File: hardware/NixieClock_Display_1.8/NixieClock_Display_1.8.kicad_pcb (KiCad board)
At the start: 2 copper layers, 31.6 x 46 mm, 2 parts, among them J1 Conn_01x14, J2 Conn_01x14

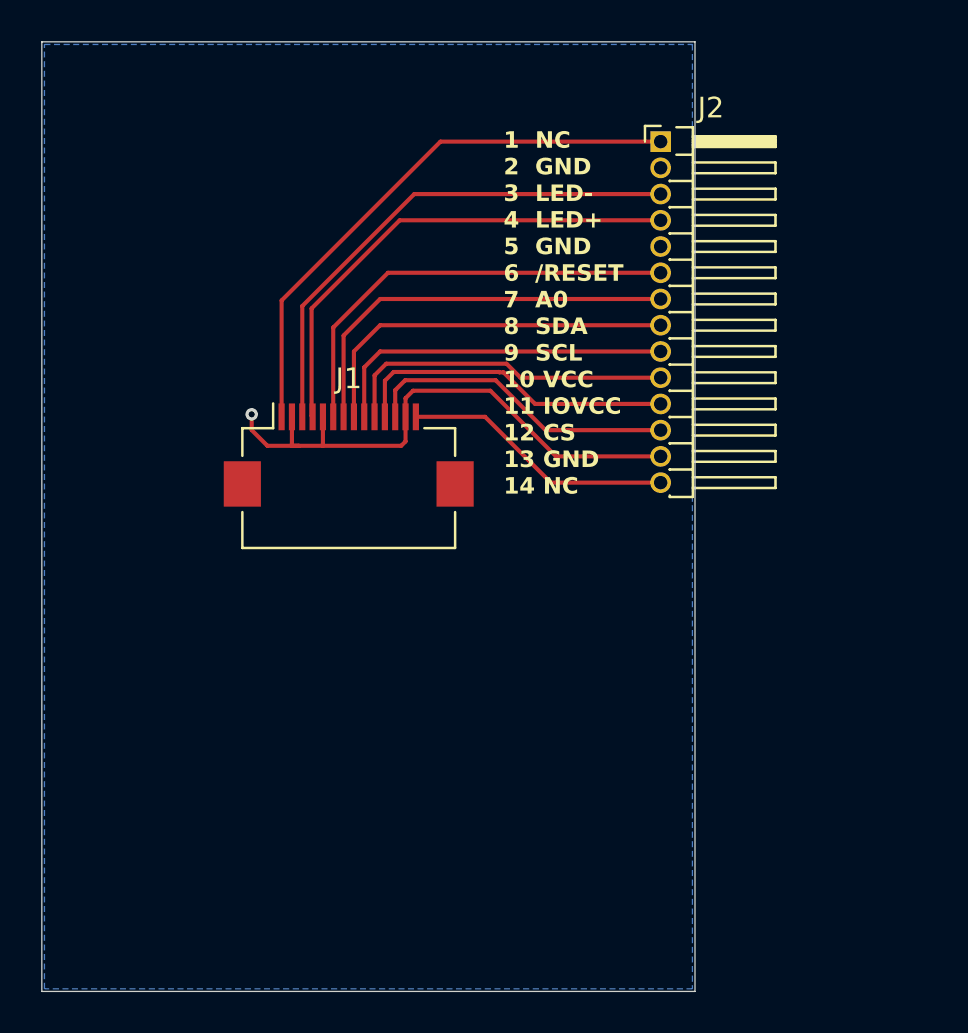
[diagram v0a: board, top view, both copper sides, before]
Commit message: schaltplan für mainboard angelegt
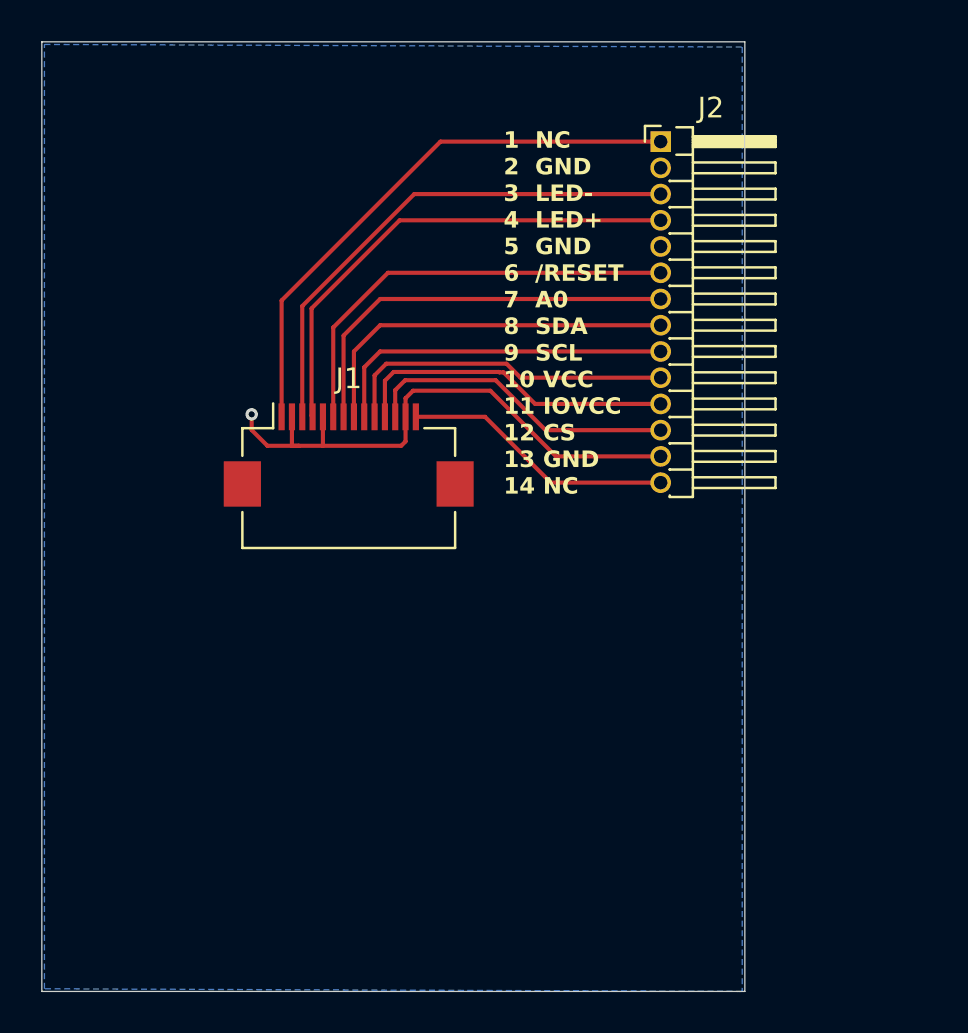
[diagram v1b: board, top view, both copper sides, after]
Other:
- board size 31.6 x 46 mm -> 34 x 46 mm
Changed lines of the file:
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@@
 	(gr_rect
 		(start 127 60.96)
-		(end 158.623 106.934)
+		(end 161.036 106.934)
 		(stroke
 			(width 0.05)
@@
 		(polygon
 			(pts
-				(xy 127.127 61.087) (xy 158.496 61.087) (xy 158.496 106.807) (xy 127.127 106.807)
+				(xy 127.127 61.087) (xy 160.909 61.214) (xy 160.909 106.934) (xy 127.127 106.807)
 			)
 		)

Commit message: update pcb. distance between fpc-connector corrected
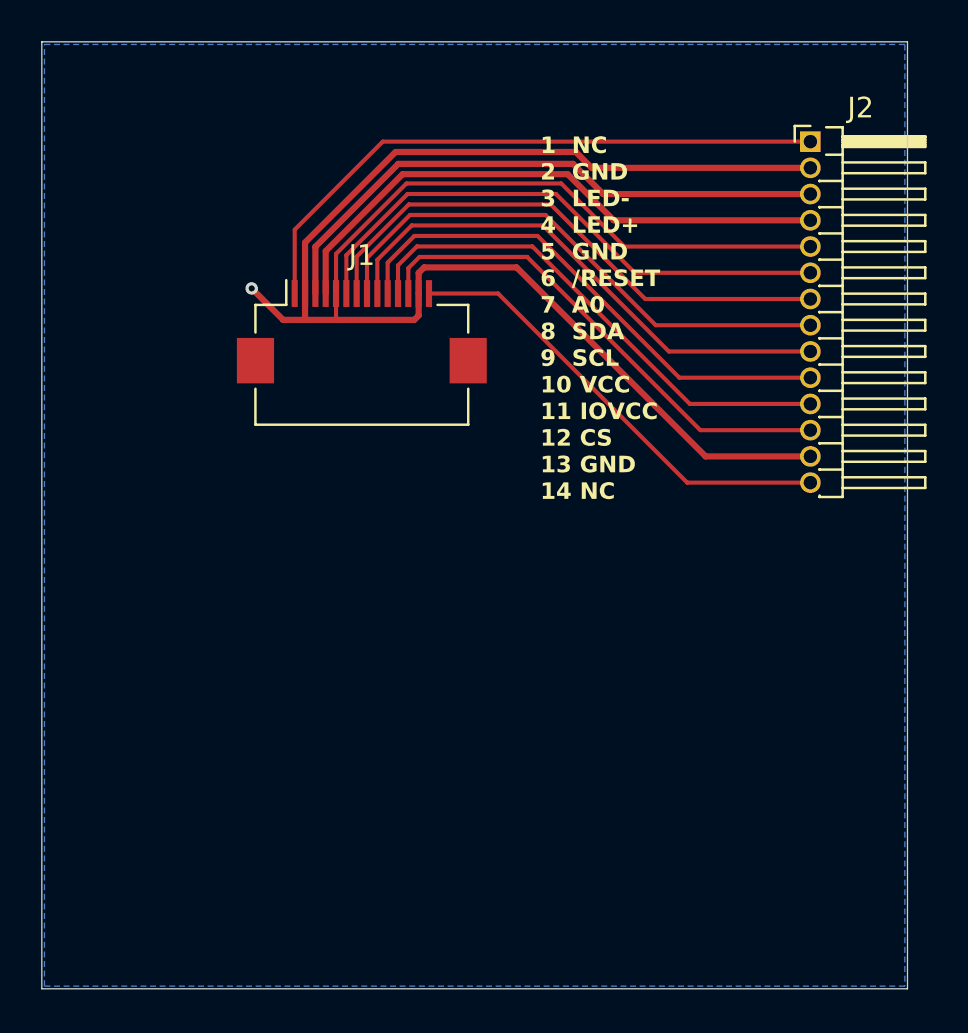
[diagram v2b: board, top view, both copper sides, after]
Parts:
- moved J2 7.25 mm to (164.2, 65.8)
- moved J1 6.00 mm to (142.5, 75.0)
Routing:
- net /GND: track 27.7 -> 93.0 mm
- net /NC.: track 13.2 -> 22.3 mm
- net /CS: track 15.3 -> 24.4 mm
- net /VCC: track 16.4 -> 25.3 mm
- net /IOVCC: track 15.9 -> 24.9 mm
- net /SCL: track 17.1 -> 25.8 mm
- net /SDA: track 18.5 -> 26.3 mm
- net /A0: track 20.0 -> 26.7 mm
- net //RES: track 21.3 -> 27.1 mm
- net /LED+: track 23.9 -> 28.0 mm
- net /LED-: track 25.0 -> 28.5 mm
- net /NC: track 27.2 -> 29.8 mm
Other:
- board size 34 x 46 mm -> 41.9 x 45.8 mm
